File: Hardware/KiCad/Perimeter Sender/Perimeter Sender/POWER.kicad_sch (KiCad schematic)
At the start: 4 parts, among them U5 TSR_1-2450

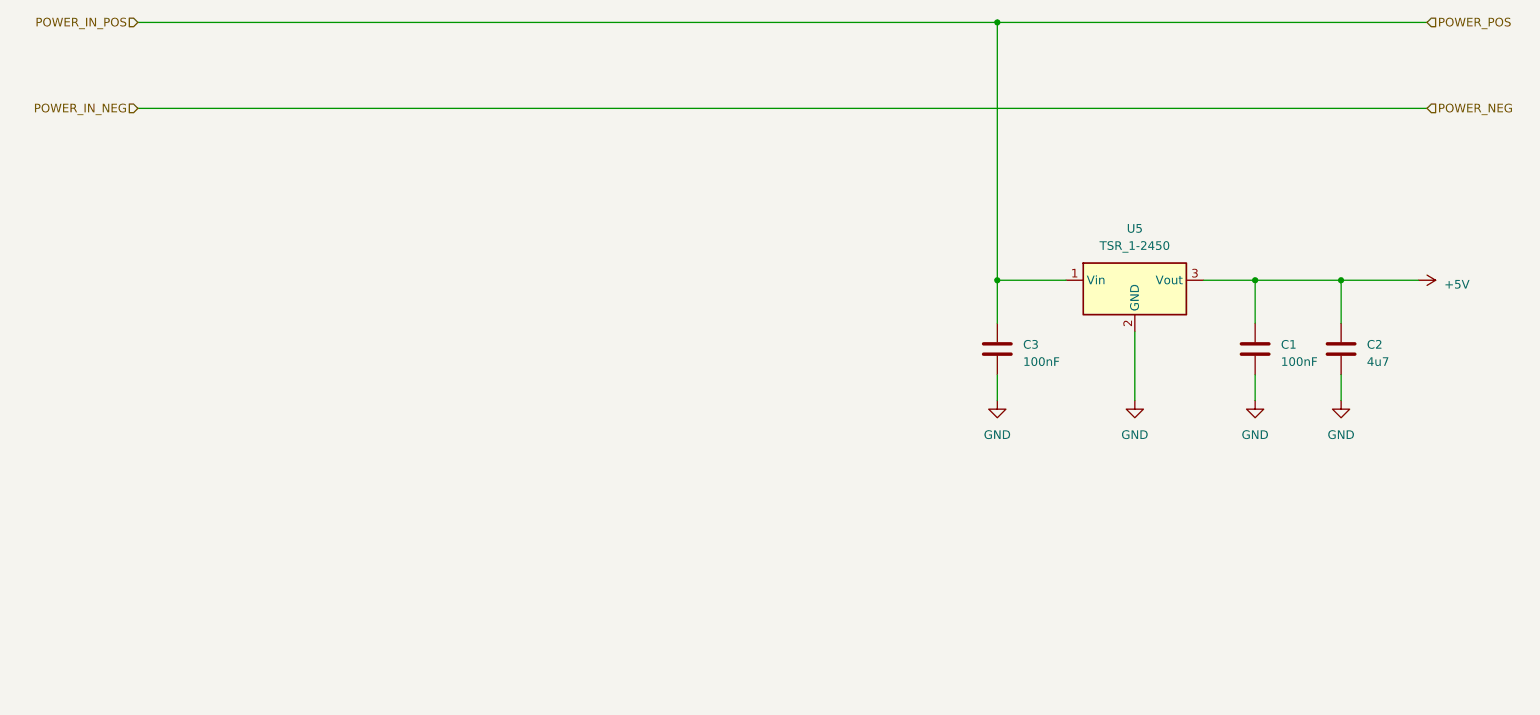
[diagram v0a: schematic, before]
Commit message: Redesign: - Controller - I2C pinning geändert - uvm
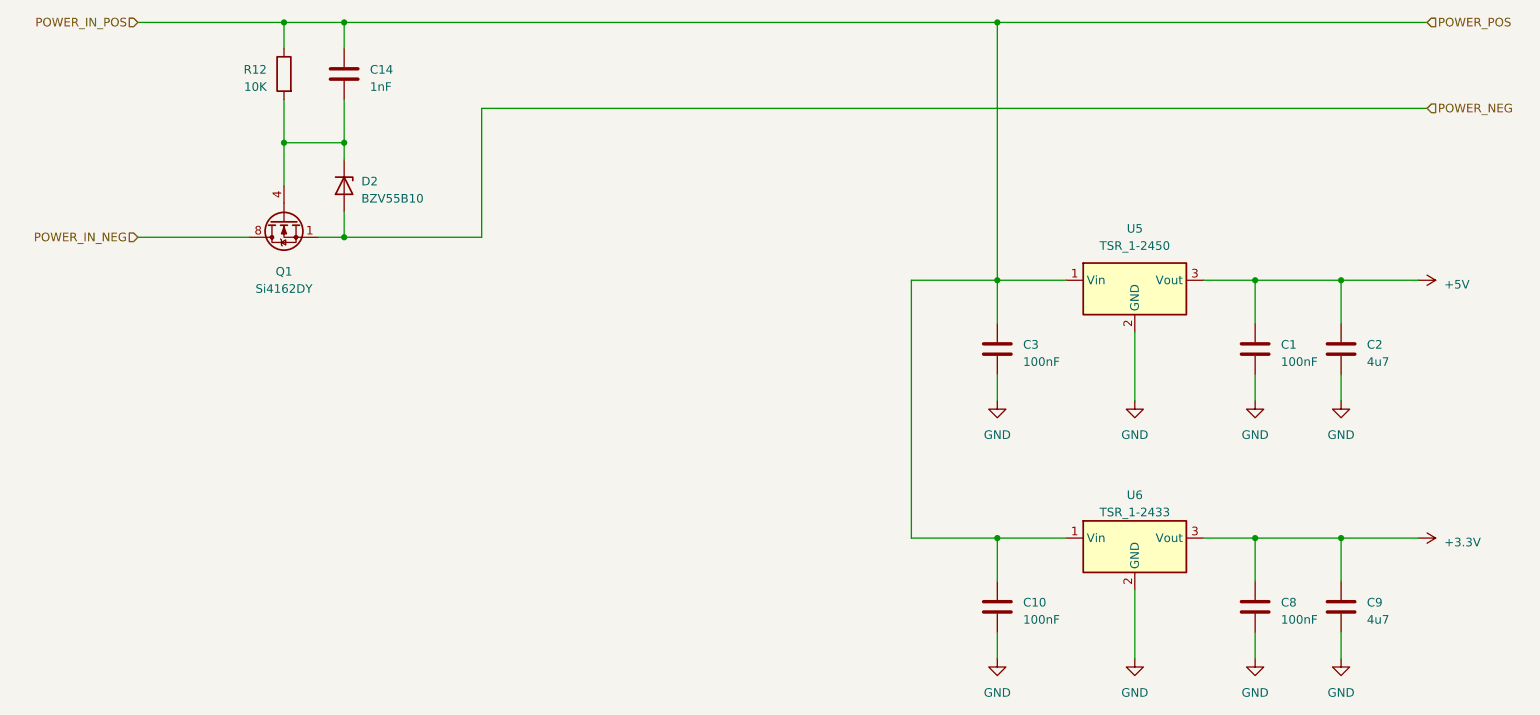
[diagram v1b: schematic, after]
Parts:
- added C10, C8: 100nF, Capacitor_SMD:C_0603_1608Metric, symbol Device:C
- added C14: 1nF, Capacitor_SMD:C_0603_1608Metric, symbol Device:C
- added C9: 4u7, Capacitor_SMD:C_0603_1608Metric, symbol Device:C
- added D2: BZV55B10, Diode_SMD:D_MiniMELF, symbol Diode:BZV55B10
- added Q1: Si4162DY, Package_SO:SOIC-8_3.9x4.9mm_P1.27mm, symbol Transistor_FET:Si4162DY
- added R12: 10K, Resistor_SMD:R_0603_1608Metric, symbol Device:R
- added U6: TSR_1-2433, Converter_DCDC:Converter_DCDC_TRACO_TSR-1_THT, symbol Regulator_Switching:TSR_1-2433
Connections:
- net GND: now also C10.2, C8.2, C9.2, U6.2 (GND)
- net POWER_IN_NEG: now also Q1.5 (D), Q1.6 (D), Q1.7 (D), Q1.8 (D)
- net POWER_IN_POS: now also C10.1, C14.1, R12.1, U6.1 (Vin)
- new net: C14.2, D2.1 (K), Q1.4 (G), R12.2
- new net +3.3V: C8.1, C9.1, U6.3 (Vout)
- new net POWER_NEG: D2.2 (A), Q1.1 (S), Q1.2 (S), Q1.3 (S)
